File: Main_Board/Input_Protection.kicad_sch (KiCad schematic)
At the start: 6 parts, among them IC1 TPS25200DRVR

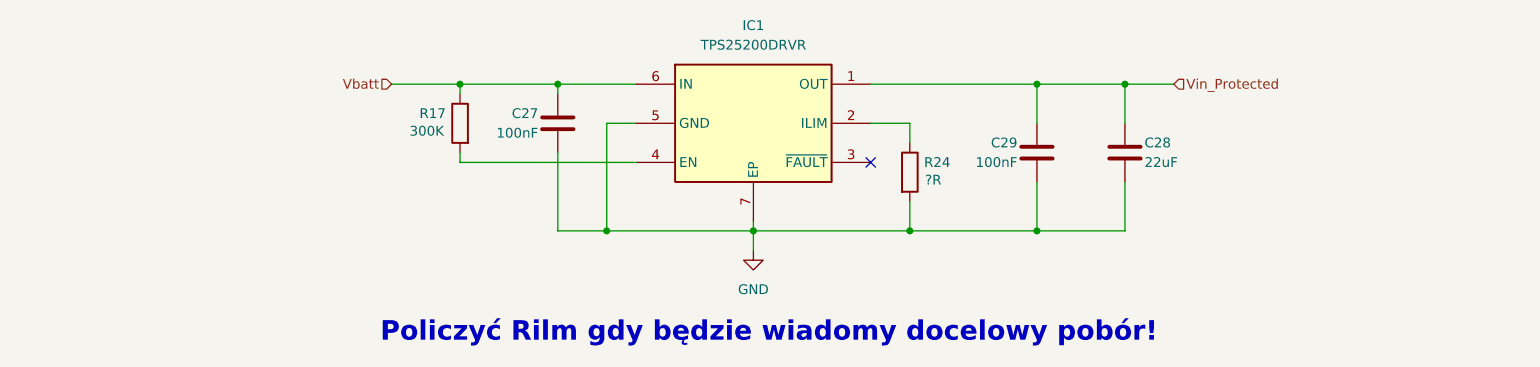
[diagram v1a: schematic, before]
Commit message: RS485 Transciever + Input Protection fix
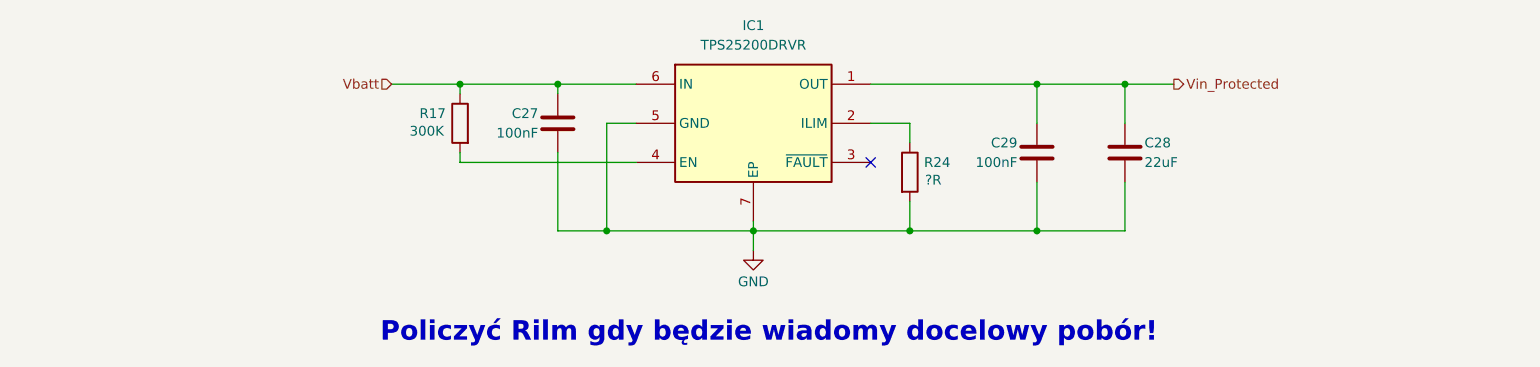
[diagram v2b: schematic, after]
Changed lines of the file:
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@@
 	)
 	(hierarchical_label "Vin_Protected"
-		(shape input)
+		(shape output)
 		(at 195.58 92.71 0)
 		(effects
@@
 		(in_pos_files yes)
 		(dnp no)
-		(fields_autoplaced yes)
 		(property "Reference" "#PWR059"
 			(at 140.97 120.65 0)
@@
 		)
 		(property "Value" "GND"
-			(at 140.97 119.38 0)
-			(show_name no)
-			(do_not_autoplace no)
+			(at 140.97 118.364 0)
+			(show_name no)
+			(do_not_autoplace no)

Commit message: Aesthetics/cleanup
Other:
- moved on the sheet: C28
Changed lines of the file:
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@@
+	)
+	(junction
+		(at 187.96 92.71)
+		(diameter 0)
+		(color 0 0 0 0)
 	)
 	(junction
@@
 	)
 	(junction
-		(at 189.23 92.71)
-		(diameter 0)
-		(color 0 0 0 0)
-	)
-	(junction
 		(at 140.97 111.76)
 		(diameter 0)
@@
 	(wire
 		(pts
-			(xy 189.23 97.79) (xy 189.23 92.71)
+			(xy 187.96 97.79) (xy 187.96 92.71)
 		)
 		(stroke
@@
 	(wire
 		(pts
-			(xy 189.23 92.71) (xy 177.8 92.71)
+			(xy 187.96 92.71) (xy 195.58 92.71)
 		)
 		(stroke
@@
 	(wire
 		(pts
-			(xy 189.23 105.41) (xy 189.23 111.76)
+			(xy 187.96 105.41) (xy 187.96 111.76)
 		)
 		(stroke
@@
 	(wire
 		(pts
-			(xy 189.23 92.71) (xy 195.58 92.71)
+			(xy 187.96 92.71) (xy 177.8 92.71)
 		)
 		(stroke
@@
 	(wire
 		(pts
-			(xy 177.8 111.76) (xy 189.23 111.76)
+			(xy 177.8 111.76) (xy 187.96 111.76)
 		)
 		(stroke
@@
 	(symbol
 		(lib_id "Device:C")
-		(at 189.23 101.6 0)
+		(at 187.96 101.6 0)
 		(unit 1)
 		(body_style 1)
@@
 		(dnp no)
 		(property "Reference" "C28"
-			(at 191.77 100.33 0)
+			(at 190.5 100.33 0)
 			(show_name no)
 			(do_not_autoplace no)
@@
 		)
 		(property "Value" "22uF"
-			(at 191.77 102.87 0)
+			(at 190.5 102.87 0)
 			(show_name no)
 			(do_not_autoplace no)
@@
 		)
 		(property "Footprint" ""
-			(at 190.1952 105.41 0)
+			(at 188.9252 105.41 0)
 			(hide yes)
 			(show_name no)
@@
 		)
 		(property "Datasheet" ""
-			(at 189.23 101.6 0)
+			(at 187.96 101.6 0)
 			(hide yes)
 			(show_name no)
@@
 		)
 		(property "Description" "Unpolarized capacitor"
-			(at 189.23 101.6 0)
-			(hide yes)
-			(show_name no)
+			(at 187.96 101.6 0)
+			(hide yes)
+			(show_name no)

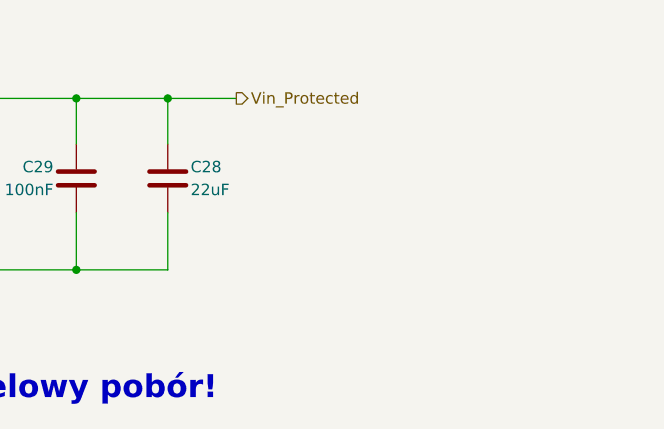
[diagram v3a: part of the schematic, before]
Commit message: add external obrds interfaces
Todo pyro chanells
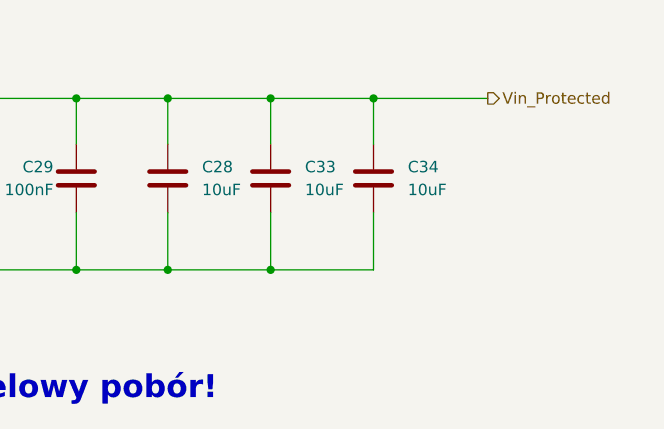
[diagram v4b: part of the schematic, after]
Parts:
- added C33, C34: 10uF, symbol Device:C
- C28: value 22uF -> 10uF
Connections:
- net GND: now also C33.2, C34.2
- net Vin_Protected: now also C33.1, C34.1

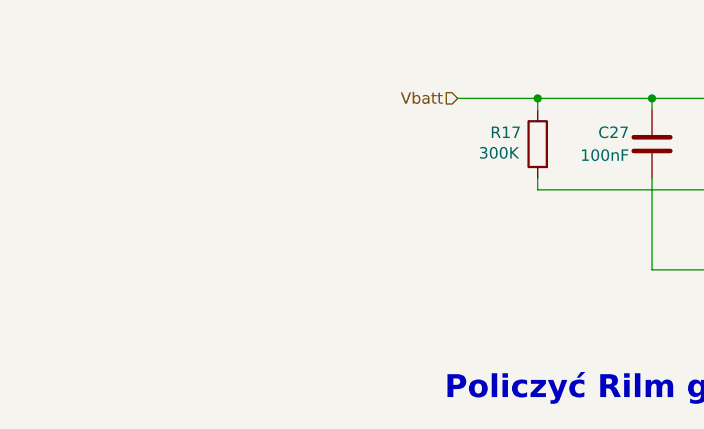
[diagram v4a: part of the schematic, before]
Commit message: Add mag sensor
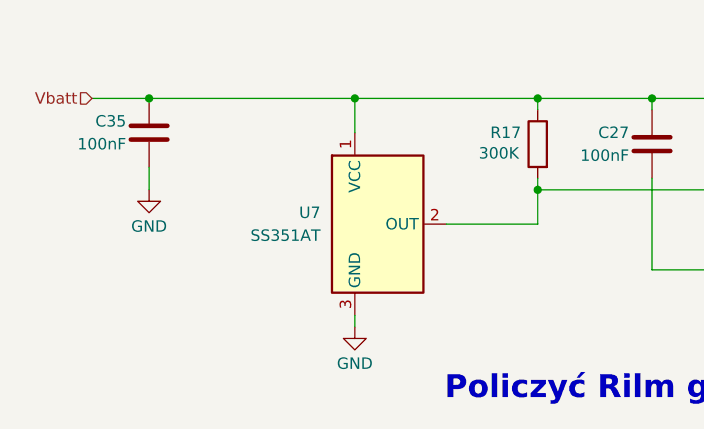
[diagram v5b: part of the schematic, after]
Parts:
- added C35: 100nF, symbol Device:C
- added U7: SS351AT, Package_TO_SOT_SMD:SOT-23, symbol Sensor_Magnetic:DRV5033AJxDBZ
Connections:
- net GND: now also C35.2, U7.3 (GND)
- net Vbatt: now also C35.1, U7.1 (VCC)
- net at IC1.4 (EN), R17.2: now also U7.2 (OUT)

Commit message: Add buzzer, Add LED, ADD R&D jumper
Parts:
- added JP1: R&D_still_on, symbol Jumper:Jumper_2_Small_Open
- renumbered C35 to C33, C27 to C34, C29 to C35, C28 to C36, C33 to C37, C34 to C38, R17 to R31, R24 to R32, U7 to U6
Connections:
- net GND: now also JP1.2 (B)
- net at IC1.4 (EN), R31.2, U6.2 (OUT): now also JP1.1 (A)
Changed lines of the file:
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@@
+	)
+	(junction
+		(at 102.87 106.68)
+		(diameter 0)
+		(color 0 0 0 0)
 	)
 	(junction
@@
 		(pts
 			(xy 199.39 92.71) (xy 210.82 92.71)
+		)
+		(stroke
+			(width 0)
+			(type default)
+		)
+	)
+	(wire
+		(pts
+			(xy 102.87 119.38) (xy 102.87 111.76)
 		)
 		(stroke
@@
 		(in_pos_files yes)
 		(dnp no)
-		(property "Reference" "R17"
+		(property "Reference" "R31"
 			(at 99.314 96.52 0)
 			(show_name no)
@@
 			(project "Main_Board"
 				(path "/7481738f-7c20-40bb-99b0-6ccd4168db33/4704f5be-58a0-4191-b01f-84980581c4a3/9c10d29b-d26a-4ccc-85ab-aaf11fc5f66b"
-					(reference "R17")
+					(reference "R31")
 					(unit 1)
 				)
@@
 		(in_pos_files yes)
 		(dnp no)
-		(property "Reference" "#PWR079"
+		(property "Reference" "#PWR084"
 			(at 82.55 124.46 0)
 			(hide yes)
@@
 			(project "Main_Board"
 				(path "/7481738f-7c20-40bb-99b0-6ccd4168db33/4704f5be-58a0-4191-b01f-84980581c4a3/9c10d29b-d26a-4ccc-85ab-aaf11fc5f66b"
-					(reference "#PWR079")
+					(reference "#PWR084")
 					(unit 1)
 				)
@@
 		(dnp no)
 		(fields_autoplaced yes)
-		(property "Reference" "U7"
+		(property "Reference" "U6"
 			(at 78.74 105.4099 0)
 			(show_name no)
@@
 			(project "Main_Board"
 				(path "/7481738f-7c20-40bb-99b0-6ccd4168db33/4704f5be-58a0-4191-b01f-84980581c4a3/9c10d29b-d26a-4ccc-85ab-aaf11fc5f66b"
-					(reference "U7")
+					(reference "U6")
 					(unit 1)
 				)
@@
 		(dnp no)
 		(fields_autoplaced yes)
-		(property "Reference" "C34"
+		(property "Reference" "C38"
 			(at 214.63 100.3299 0)
 			(show_name no)
@@
 			(project "Main_Board"
 				(path "/7481738f-7c20-40bb-99b0-6ccd4168db33/4704f5be-58a0-4191-b01f-84980581c4a3/9c10d29b-d26a-4ccc-85ab-aaf11fc5f66b"
-					(reference "C34")
+					(reference "C38")
 					(unit 1)
 				)
@@
 		(in_pos_files yes)
 		(dnp no)
-		(property "Reference" "#PWR080"
+		(property "Reference" "#PWR083"
 			(at 59.69 109.22 0)
 			(hide yes)
@@
 			(project "Main_Board"
 				(path "/7481738f-7c20-40bb-99b0-6ccd4168db33/4704f5be-58a0-4191-b01f-84980581c4a3/9c10d29b-d26a-4ccc-85ab-aaf11fc5f66b"
-					(reference "#PWR080")
+					(reference "#PWR083")
 					(unit 1)
 				)
@@
 		(in_pos_files yes)
 		(dnp no)
-		(property "Reference" "C29"
+		(property "Reference" "C35"
 			(at 175.26 100.33 0)
 			(show_name no)
@@
 			(project "Main_Board"
 				(path "/7481738f-7c20-40bb-99b0-6ccd4168db33/4704f5be-58a0-4191-b01f-84980581c4a3/9c10d29b-d26a-4ccc-85ab-aaf11fc5f66b"
-					(reference "C29")
+					(reference "C35")
 					(unit 1)
 				)
@@
 		(dnp no)
 		(fields_autoplaced yes)
-		(property "Reference" "C28"
+		(property "Reference" "C36"
 			(at 191.77 100.3299 0)
 			(show_name no)
@@
 			(project "Main_Board"
 				(path "/7481738f-7c20-40bb-99b0-6ccd4168db33/4704f5be-58a0-4191-b01f-84980581c4a3/9c10d29b-d26a-4ccc-85ab-aaf11fc5f66b"
-					(reference "C28")
+					(reference "C36")
 					(unit 1)
 				)
@@
 		(in_pos_files yes)
 		(dnp no)
-		(property "Reference" "C35"
+		(property "Reference" "C33"
 			(at 57.15 95.25 0)
 			(show_name no)
@@
 			(project "Main_Board"
 				(path "/7481738f-7c20-40bb-99b0-6ccd4168db33/4704f5be-58a0-4191-b01f-84980581c4a3/9c10d29b-d26a-4ccc-85ab-aaf11fc5f66b"
-					(reference "C35")
+					(reference "C33")
 					(unit 1)
 				)
@@
 		(in_pos_files yes)
 		(dnp no)
-		(property "Reference" "C27"
+		(property "Reference" "C34"
 			(at 113.03 96.52 0)
 			(show_name no)
@@
 			(project "Main_Board"
 				(path "/7481738f-7c20-40bb-99b0-6ccd4168db33/4704f5be-58a0-4191-b01f-84980581c4a3/9c10d29b-d26a-4ccc-85ab-aaf11fc5f66b"
-					(reference "C27")
+					(reference "C34")
 					(unit 1)
 				)
@@
 		(in_pos_files yes)
 		(dnp no)
-		(property "Reference" "R24"
+		(property "Reference" "R32"
 			(at 164.846 102.87 0)
 			(show_name no)
@@
 			(project "Main_Board"
 				(path "/7481738f-7c20-40bb-99b0-6ccd4168db33/4704f5be-58a0-4191-b01f-84980581c4a3/9c10d29b-d26a-4ccc-85ab-aaf11fc5f66b"
-					(reference "R24")
+					(reference "R32")
+					(unit 1)
+				)
+			)
+		)
+	)
+	(symbol
+		(lib_id "power:GND")
+		(at 102.87 119.38 0)
+		(unit 1)
+		(body_style 1)
+		(exclude_from_sim no)
+		(in_bom yes)
+		(on_board yes)
+		(in_pos_files yes)
+		(dnp no)
+		(property "Reference" "#PWR085"
+			(at 102.87 125.73 0)
+			(hide yes)
+			(show_name no)
+			(do_not_autoplace no)
+			(effects
+				(font
+					(size 1.27 1.27)
+				)
+			)
+		)
+		(property "Value" "GND"
+			(at 102.87 123.444 0)
+			(show_name no)
+			(do_not_autoplace no)
+			(effects
+				(font
+					(size 1.27 1.27)
+				)
+			)
+		)
+		(property "Footprint" ""
+			(at 102.87 119.38 0)
+			(hide yes)
+			(show_name no)
+			(do_not_autoplace no)
+			(effects
+				(font
+					(size 1.27 1.27)
+				)
+			)
+		)
+		(property "Datasheet" ""
+			(at 102.87 119.38 0)
+			(hide yes)
+			(show_name no)
+			(do_not_autoplace no)
+			(effects
+				(font
+					(size 1.27 1.27)
+				)
+			)
+		)
+		(property "Description" "Power symbol creates a global label with name \"GND\" , ground"
+			(at 102.87 119.38 0)
+			(hide yes)
+			(show_name no)
+			(do_not_autoplace no)
+			(effects
+				(font
+					(size 1.27 1.27)
+				)
+			)
+		)
+		(pin "1"
+		)
+		(instances
+			(project "Main_Board"
+				(path "/7481738f-7c20-40bb-99b0-6ccd4168db33/4704f5be-58a0-4191-b01f-84980581c4a3/9c10d29b-d26a-4ccc-85ab-aaf11fc5f66b"
+					(reference "#PWR085")
 					(unit 1)
 				)
@@
 		(in_pos_files yes)
 		(dnp no)
-		(property "Reference" "#PWR059"
+		(property "Reference" "#PWR086"
 			(at 140.97 120.65 0)
 			(hide yes)
@@
 			(project "Main_Board"
 				(path "/7481738f-7c20-40bb-99b0-6ccd4168db33/4704f5be-58a0-4191-b01f-84980581c4a3/9c10d29b-d26a-4ccc-85ab-aaf11fc5f66b"
-					(reference "#PWR059")
+					(reference "#PWR086")
 					(unit 1)
 				)
@@
 		(dnp no)
 		(fields_autoplaced yes)
-		(property "Reference" "C33"
+		(property "Reference" "C37"
 			(at 203.2 100.3299 0)
 			(show_name no)
@@
 			(project "Main_Board"
 				(path "/7481738f-7c20-40bb-99b0-6ccd4168db33/4704f5be-58a0-4191-b01f-84980581c4a3/9c10d29b-d26a-4ccc-85ab-aaf11fc5f66b"
-					(reference "C33")
+					(reference "C37")
 					(unit 1)
 				)
+			)
+		)
+	)
+	(symbol
+		(lib_id "Jumper:Jumper_2_Small_Open")
+		(at 102.87 109.22 270)
+		(unit 1)
+		(body_style 1)
+		(exclude_from_sim no)
+		(in_bom yes)
+		(on_board yes)
+		(in_pos_files yes)
+		(dnp no)
+		(property "Reference" "JP1"
+			(at 103.378 112.268 90)
+			(show_name no)
+			(do_not_autoplace no)
+			(effects
+				(font
+					(size 1.27 1.27)
+				)
+				(justify left)
+			)
+		)
+		(property "Value" "R&D_still_on"
+			(at 103.378 114.808 90)
+			(show_name no)
+			(do_not_autoplace no)
+			(effects
+				(font
+					(size 1.27 1.27)
+				)
+				(justify left)
+			)
+		)
+		(property "Footprint" ""
+			(at 102.87 109.22 0)
+			(hide yes)
+			(show_name no)
+			(do_not_autoplace no)
+			(effects
+				(font
+					(size 1.27 1.27)
+				)
+			)
+		)
+		(property "Datasheet" ""
+			(at 102.87 109.22 0)
+			(hide yes)
+			(show_name no)
+			(do_not_autoplace no)
+			(effects
+				(font
+					(size 1.27 1.27)
+				)
+			)
+		)
+		(property "Description" "Jumper, 2-pole, small symbol, open"
+			(at 102.87 109.22 0)
+			(hide yes)
+			(show_name no)
+			(do_not_autoplace no)
+			(effects
+				(font
+					(size 1.27 1.27)
+				)
+			)
+		)
+		(pin "1"
+		)
+		(pin "2"
+		)
+		(instances
+			(project "Main_Board"
+				(path "/7481738f-7c20-40bb-99b0-6ccd4168db33/4704f5be-58a0-4191-b01f-84980581c4a3/9c10d29b-d26a-4ccc-85ab-aaf11fc5f66b"
+					(reference "JP1")
+					(unit 1)
+				)

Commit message: ADD footprints
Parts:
- C33, C34, C35, C36, C37, C38: footprint (none) -> Capacitor_SMD:C_0603_1608Metric
- JP1: footprint (none) -> Jumper:SolderJumper-2_P1.3mm_Open_RoundedPad1.0x1.5mm
- R31: footprint (none) -> Resistor_SMD:R_0603_1608Metric
- R32: value ?R -> 39k; footprint (none) -> Resistor_SMD:R_0603_1608Metric
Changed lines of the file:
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@@
 			)
 		)
-		(property "Footprint" ""
+		(property "Footprint" "Resistor_SMD:R_0603_1608Metric"
 			(at 104.648 97.79 90)
 			(hide yes)
@@
 			)
 		)
-		(property "Footprint" ""
+		(property "Footprint" "Capacitor_SMD:C_0603_1608Metric"
 			(at 211.7852 105.41 0)
 			(hide yes)
@@
 			)
 		)
-		(property "Footprint" ""
+		(property "Footprint" "Capacitor_SMD:C_0603_1608Metric"
 			(at 176.8348 105.41 0)
 			(hide yes)
@@
 			)
 		)
-		(property "Footprint" ""
+		(property "Footprint" "Capacitor_SMD:C_0603_1608Metric"
 			(at 188.9252 105.41 0)
 			(hide yes)
@@
 			)
 		)
-		(property "Footprint" ""
+		(property "Footprint" "Capacitor_SMD:C_0603_1608Metric"
 			(at 58.7248 100.33 0)
 			(hide yes)
@@
 			)
 		)
-		(property "Footprint" ""
+		(property "Footprint" "Capacitor_SMD:C_0603_1608Metric"
 			(at 114.6048 101.6 0)
 			(hide yes)
@@
 			)
 		)
-		(property "Value" "?R"
+		(property "Value" "39k"
 			(at 164.338 105.156 0)
 			(show_name no)
@@
 			)
 		)
-		(property "Footprint" ""
+		(property "Footprint" "Resistor_SMD:R_0603_1608Metric"
 			(at 159.512 104.14 90)
 			(hide yes)
@@
 			)
 		)
-		(property "Footprint" ""
+		(property "Footprint" "Capacitor_SMD:C_0603_1608Metric"
 			(at 200.3552 105.41 0)
 			(hide yes)
@@
 			)
 		)
-		(property "Footprint" ""
+		(property "Footprint" "Jumper:SolderJumper-2_P1.3mm_Open_RoundedPad1.0x1.5mm"
 			(at 102.87 109.22 0)
 			(hide yes)

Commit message: Add pyro channels x2
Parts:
- renumbered R31 to R33, R32 to R34
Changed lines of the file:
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@@
 		(in_pos_files yes)
 		(dnp no)
-		(property "Reference" "R31"
+		(property "Reference" "R33"
 			(at 99.314 96.52 0)
 			(show_name no)
@@
 			(project "Main_Board"
 				(path "/7481738f-7c20-40bb-99b0-6ccd4168db33/4704f5be-58a0-4191-b01f-84980581c4a3/9c10d29b-d26a-4ccc-85ab-aaf11fc5f66b"
-					(reference "R31")
+					(reference "R33")
 					(unit 1)
 				)
@@
 		(in_pos_files yes)
 		(dnp no)
-		(property "Reference" "#PWR084"
+		(property "Reference" "#PWR088"
 			(at 82.55 124.46 0)
 			(hide yes)
@@
 			(project "Main_Board"
 				(path "/7481738f-7c20-40bb-99b0-6ccd4168db33/4704f5be-58a0-4191-b01f-84980581c4a3/9c10d29b-d26a-4ccc-85ab-aaf11fc5f66b"
-					(reference "#PWR084")
+					(reference "#PWR088")
 					(unit 1)
 				)
@@
 		(in_pos_files yes)
 		(dnp no)
-		(property "Reference" "#PWR083"
+		(property "Reference" "#PWR087"
 			(at 59.69 109.22 0)
 			(hide yes)
@@
 			(project "Main_Board"
 				(path "/7481738f-7c20-40bb-99b0-6ccd4168db33/4704f5be-58a0-4191-b01f-84980581c4a3/9c10d29b-d26a-4ccc-85ab-aaf11fc5f66b"
-					(reference "#PWR083")
+					(reference "#PWR087")
 					(unit 1)
 				)
@@
 		(in_pos_files yes)
 		(dnp no)
-		(property "Reference" "R32"
+		(property "Reference" "R34"
 			(at 164.846 102.87 0)
 			(show_name no)
@@
 			(project "Main_Board"
 				(path "/7481738f-7c20-40bb-99b0-6ccd4168db33/4704f5be-58a0-4191-b01f-84980581c4a3/9c10d29b-d26a-4ccc-85ab-aaf11fc5f66b"
-					(reference "R32")
+					(reference "R34")
 					(unit 1)
 				)
@@
 		(in_pos_files yes)
 		(dnp no)
-		(property "Reference" "#PWR085"
+		(property "Reference" "#PWR089"
 			(at 102.87 125.73 0)
 			(hide yes)
@@
 			(project "Main_Board"
 				(path "/7481738f-7c20-40bb-99b0-6ccd4168db33/4704f5be-58a0-4191-b01f-84980581c4a3/9c10d29b-d26a-4ccc-85ab-aaf11fc5f66b"
-					(reference "#PWR085")
+					(reference "#PWR089")
 					(unit 1)
 				)
@@
 		(in_pos_files yes)
 		(dnp no)
-		(property "Reference" "#PWR086"
+		(property "Reference" "#PWR090"
 			(at 140.97 120.65 0)
 			(hide yes)
@@
 			(project "Main_Board"
 				(path "/7481738f-7c20-40bb-99b0-6ccd4168db33/4704f5be-58a0-4191-b01f-84980581c4a3/9c10d29b-d26a-4ccc-85ab-aaf11fc5f66b"
-					(reference "#PWR086")
-					(unit 1)
-				)
+					(reference "#PWR090")
+					(unit 1)
+				)
